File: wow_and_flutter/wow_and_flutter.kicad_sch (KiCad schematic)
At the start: 72 parts, among them J1 EURO POWER, J2 OUTPUT, J3 B1_POWER, J4 B2_POWER, J5 B1_SIGNAL, J6 B2_SIGNAL, Q1 2N3904, Q2 J113, Q3 2N3904, SW1 SW_SPDT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

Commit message: Complete PCB laout
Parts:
- C3, C4, C5, C6: value 0.1uF -> 100nF
- J5: footprint Connector_PinHeader_2.54mm:PinHeader_1x07_P2.54mm_Vertical -> Connector_PinHeader_2.54mm:PinHeader_1x06_P2.54mm_Vertical; symbol Connector_Generic:Conn_01x07 -> Connector_Generic:Conn_01x06
- J6: footprint Connector_PinSocket_2.54mm:PinSocket_1x07_P2.54mm_Vertical -> Connector_PinSocket_2.54mm:PinSocket_1x06_P2.54mm_Vertical; symbol Connector_Generic:Conn_01x07 -> Connector_Generic:Conn_01x06
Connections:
- net +12V: now also C3.2, C5.2; no longer C3.1, C5.1
- net DEPTH_CTRL: now also J5.3 (Pin_3), J6.3 (Pin_3), U2.3 (+); no longer J5.4 (Pin_4), J6.4 (Pin_4), U2.10 (+)
- net DEPTH_FB: now also J5.2 (Pin_2), J6.2 (Pin_2); no longer J5.3 (Pin_3), J6.3 (Pin_3)
- net GND: now also C3.1, C5.1, U2.5 (+), U2.9 (-); no longer C3.2, C5.2, U2.3 (+), U2.6 (-)
- net LFO_CTRL: now also J5.6 (Pin_6), J6.6 (Pin_6), U2.6 (-); no longer J5.7 (Pin_7), J6.7 (Pin_7), U2.2 (-)
- net LFO_FB: now also J5.5 (Pin_5), J6.5 (Pin_5); no longer J5.6 (Pin_6), J6.6 (Pin_6)
- net S&H: now also J5.4 (Pin_4), J6.4 (Pin_4), U1.8; no longer J5.2 (Pin_2), J6.2 (Pin_2), U1.14
- net SH_TRIG: now also U1.14; no longer U1.8
- net SLEW_OUT: no longer J5.5 (Pin_5), J6.5 (Pin_5)
- net SQR: now also U2.8; no longer U2.7
- net TRI: now also U2.7; no longer U2.1
- net NOISE_AMP1: now reaches C10.1, C9.2, R10.2, U1.1
- net NOISE_AMP1_FB: now reaches C9.1, R10.1, R9.2, U1.2 (-)
- net NOISE_IN: now reaches C8.2, R8.1, U1.3 (+)
- net SH_GATE: now reaches D2.2 (A), Q2.3 (G), R17.2
- net TRIG_FILTER: now reaches C12.1, D1.2 (A), R13.1
- net SH_IN: now reaches C13.2, Q2.2 (S)
- net SH_IN: now also U1.10 (+); no longer U1.12 (+)
- net SH_FB: now reaches C14.1, R18.2, R19.1
- net SH_FB: now also U1.9 (-); no longer U1.13 (-)
- net GAIN_SELECT: now reaches C16.2, JP1.4 (C), R20.2, U2.13 (-)
- net LFO_CMP: now reaches R3.2, R4.1
- net LFO_CMP: now also U2.10 (+); no longer U2.5 (+)
- net TRIG_CMP: now reaches R15.2, R16.1
- net TRIG_CMP: now also U1.13 (-); no longer U1.9 (-)
- net NOISE_AMP2_FB: now reaches C11.1, R12.1, RV2.1, U1.6 (-)
- net NOISE_AMP2: now reaches C10.2, R11.1, U1.5 (+)
- net NOISE_SRC: now reaches C8.1, Q1.1 (E), R7.2
- net TRIG_IN: now reaches D1.1 (K), R14.1
- net TRIG_IN: now also U1.12 (+); no longer U1.10 (+)
- new net INV_OUT: R20.1, U2.1, U2.2 (-)
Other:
- moved on the sheet: C1, U1C, U1D, U2A, U2B, U2C

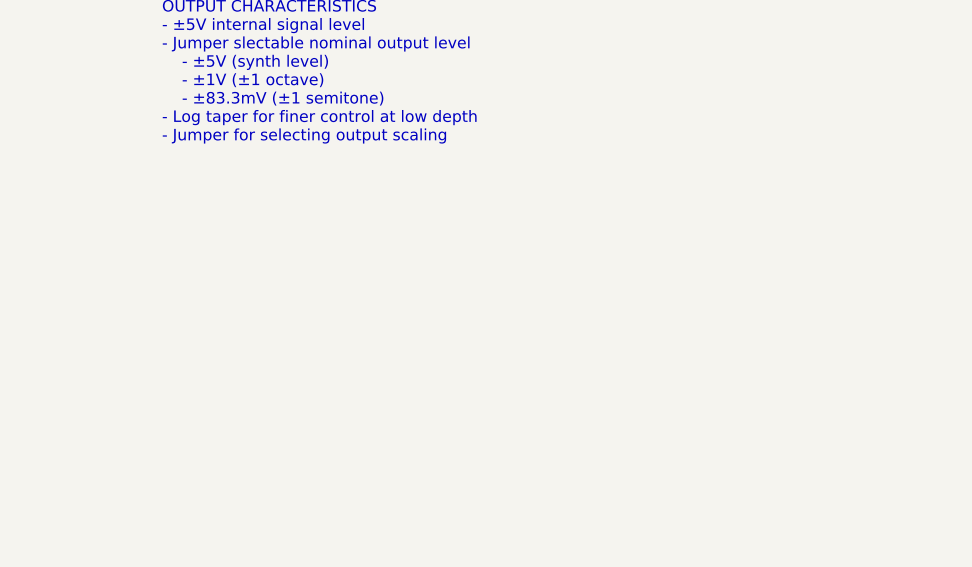
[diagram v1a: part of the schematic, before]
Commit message: Add list of issues on schematic
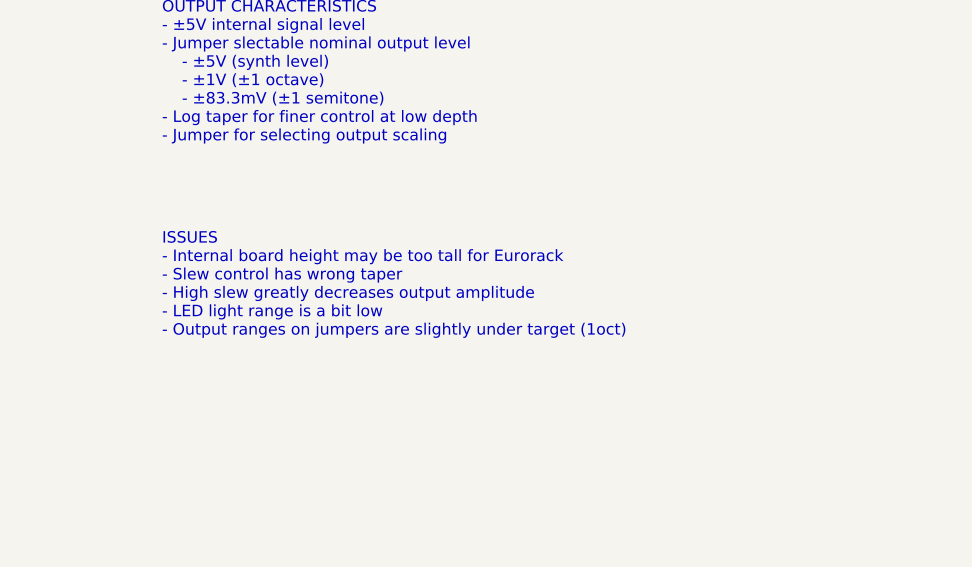
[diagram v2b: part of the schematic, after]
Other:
- note added: "ISSUES - Internal board height may be too tall for Eurorack - Slew control has wrong taper - High slew greatly decreases output amplitude - LED light range is a bit low - Output ranges on jumpers are slightly under target (1oct)"
